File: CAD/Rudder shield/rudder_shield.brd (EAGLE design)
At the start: 41.5 x 35.4 mm, 8 parts

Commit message: Added a value for the capacitor for the lowpass filter.
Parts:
- C1: value (none) -> 1uF
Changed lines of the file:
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@@
 <attribute name="NAME" x="40.64" y="21.0185" size="1.143" layer="25" ratio="14"/>
 </element>
-<element name="C1" library="ASL" package="1206" value="" x="37.465" y="21.59" smashed="yes" rot="R90">
+<element name="C1" library="ASL" package="1206" value="1uF" x="37.465" y="21.59" smashed="yes" rot="R90">
 <attribute name="NAME" x="38.608" y="25.4" size="1.143" layer="25" ratio="14" rot="R180"/>
 <attribute name="VALUE" x="38.989" y="20.193" size="0.4064" layer="27" rot="R90"/>

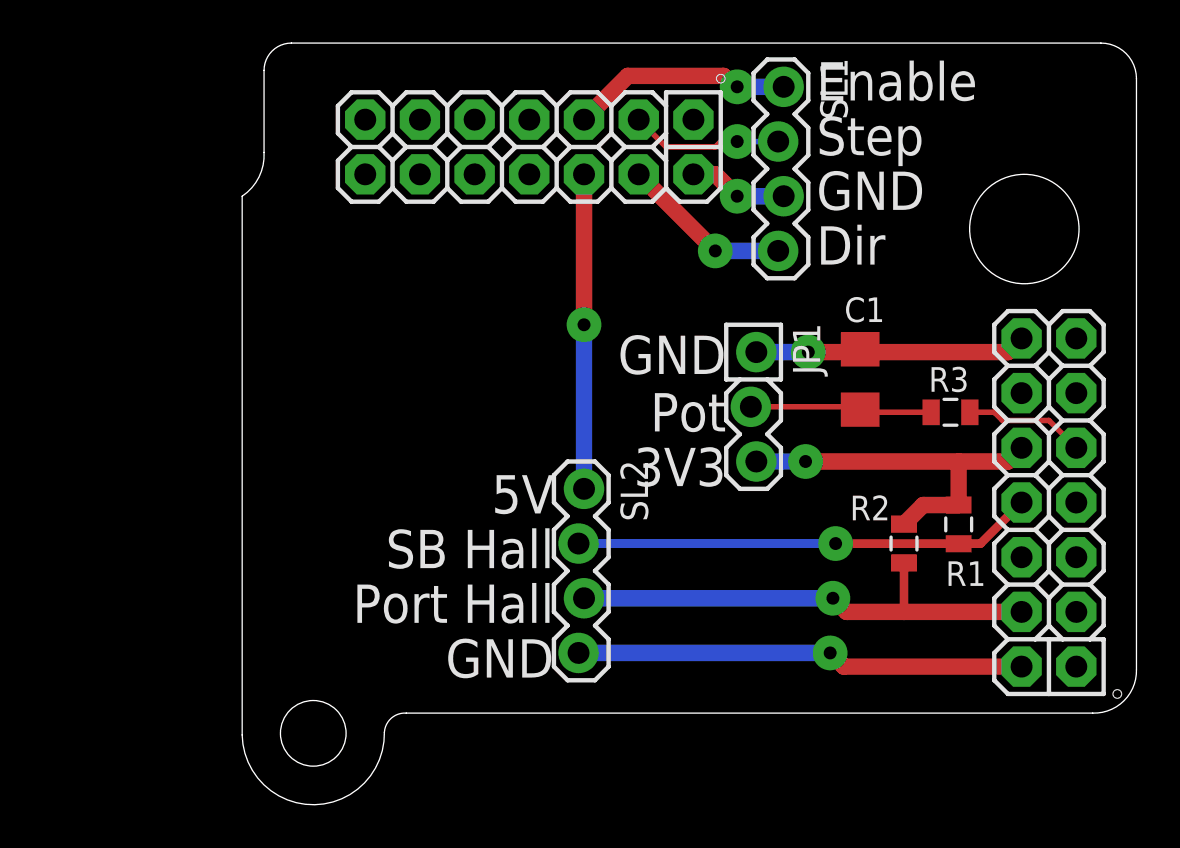
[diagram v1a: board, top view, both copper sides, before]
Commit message: Updated the control and rudder shields to be single-sided on the top for a board run. Also updated their documentation.
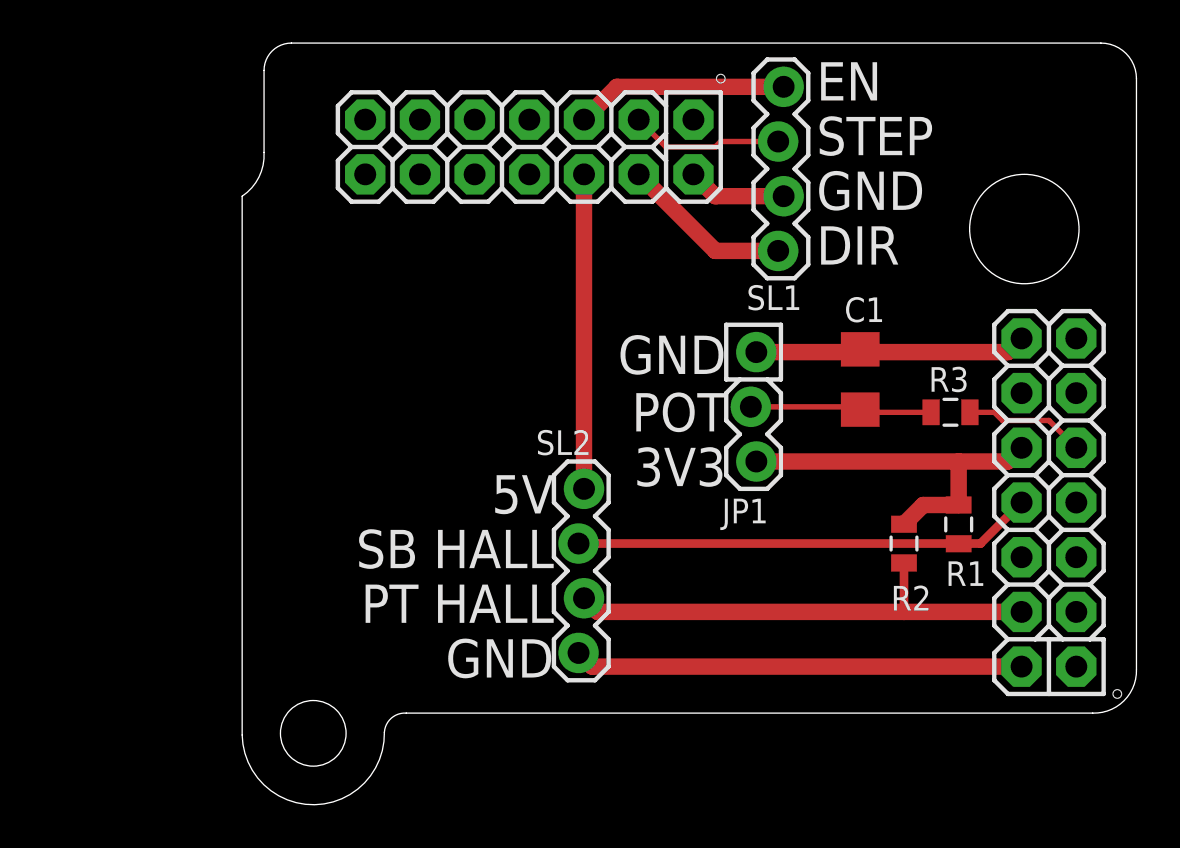
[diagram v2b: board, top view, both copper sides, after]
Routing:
- net EN: track 10.3 -> 9.90 mm, vias 1 -> 0
- net GND14: track 12.7 -> 12.8 mm, vias 1 -> 0
- net SB_HALL: vias 1 -> 0
- net GND16: vias 1 -> 0
- net STEP: vias 1 -> 0
- net PT_HALL: vias 1 -> 0
- net GND2: vias 1 -> 0
- net DIR: vias 1 -> 0
- net 5V0: vias 1 -> 0
- net 3V310: vias 1 -> 0
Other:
- board text added: "DIR"
- board text added: "EN"
- board text added: "POT"
- board text added: "PT HALL"
- board text added: "SB HALL"
- board text added: "STEP"
- board text removed: "Dir"
- board text removed: "Enable"
- board text removed: "Port Hall"
- board text removed: "Pot"
- board text removed: "SB Hall"
- board text removed: "Step"

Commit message: Updated the rudder shield to the new v3 CANode shield design.
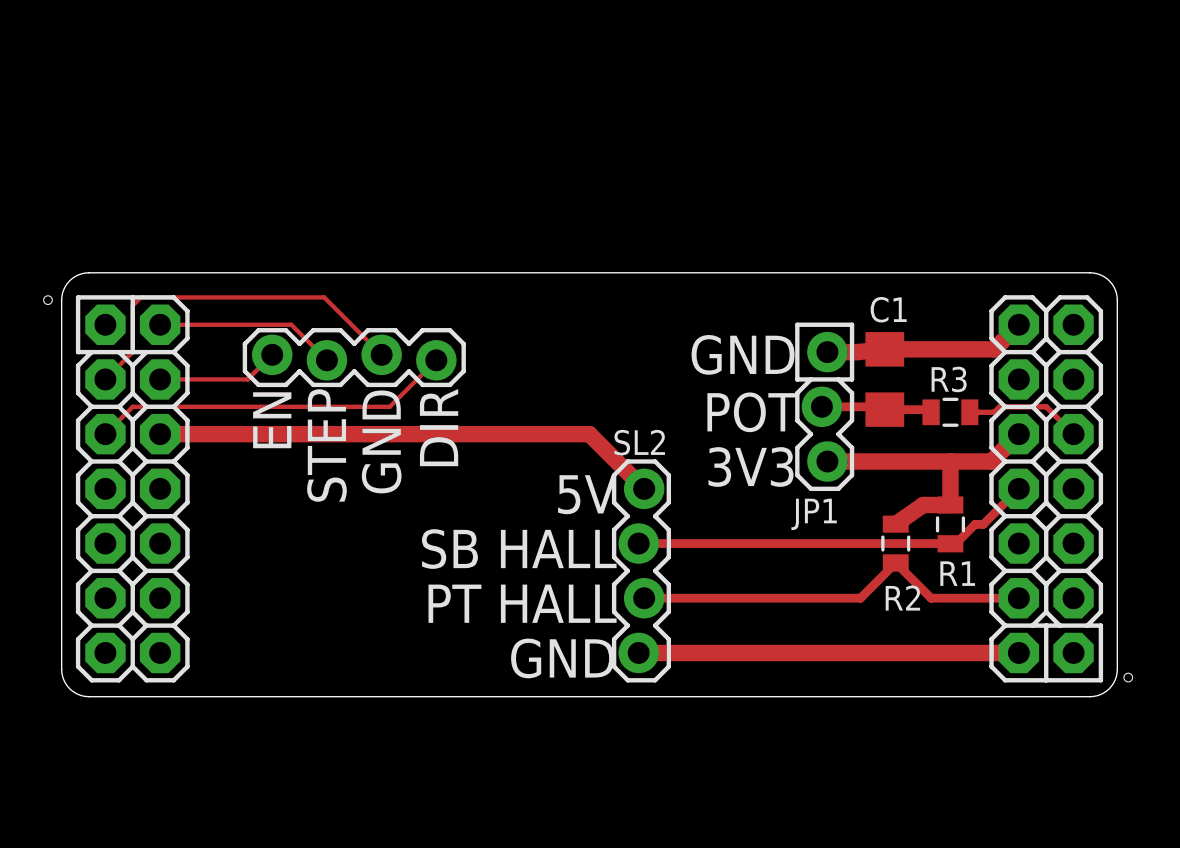
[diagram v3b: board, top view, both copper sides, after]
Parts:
- U$1: value CAN_NODE_SHIELD -> CANODE_SHIELD; device ASL:CAN_NODE_SHIELD -> ASL:CANODE_SHIELD
- moved SL1 20.4 mm to (17.8, 22.6), turned to 180 degrees
- moved JP1 3.30 mm to (35.8, 22.9)
- moved SL2 2.79 mm to (27.3, 16.5)
- moved C1 1.14 mm to (38.6, 21.6)
- moved R1 0.38 mm to (41.7, 14.9)
- moved R2 0.38 mm to (39.1, 14.0)
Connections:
- net 3V310: now also U$1.3V3; no longer U$1.P$10
- net 5V0: now also U$1.5V1; no longer U$1.P$20
- net DIR: now also U$1.RB9; no longer U$1.P$18
- net EN: now also U$1.RB10; no longer U$1.P$19
- net GND14: now also U$1.GND; no longer U$1.P$14
- net GND16: now also U$1.GND6; no longer U$1.P$16
- net GND2: now also U$1.GND2; no longer U$1.P$2
- net POT: now also U$1.RB2; no longer U$1.P$9
- net PT_HALL: now also U$1.A0; no longer U$1.P$4
- net SB_HALL: now also U$1.RB1; no longer U$1.P$8
- net STEP: now also U$1.RB12; no longer U$1.P$17
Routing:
- net STEP: track 7.11 -> 16.8 mm
- net 5V0: track 14.6 -> 23.5 mm
- net EN: track 9.90 -> 16.8 mm
- net PT_HALL: track 22.9 -> 18.8 mm
- net GND16: track 4.61 -> 8.43 mm
- net 3V310: track 17.5 -> 14.3 mm
- net GND2: track 20.8 -> 17.7 mm
- net N$1: track 8.66 -> 5.94 mm
- net SB_HALL: track 21.5 -> 19.0 mm
- net DIR: track 7.95 -> 5.68 mm
- net GND14: track 12.8 -> 10.5 mm
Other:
- board size 41.5 x 35.4 mm -> 49 x 19.7 mm
